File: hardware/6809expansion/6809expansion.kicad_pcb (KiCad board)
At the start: 2 copper layers, 99.7 x 99.7 mm, 13 parts, among them J0 SS50-LIKE, J1 SS50-LIKE, J2 SS50-LIKE, J3 SS50-LIKE, J4 SS50-LIKE, J5 SS50-LIKE, J6 SS50-LIKE, J7 SS50-LIKE

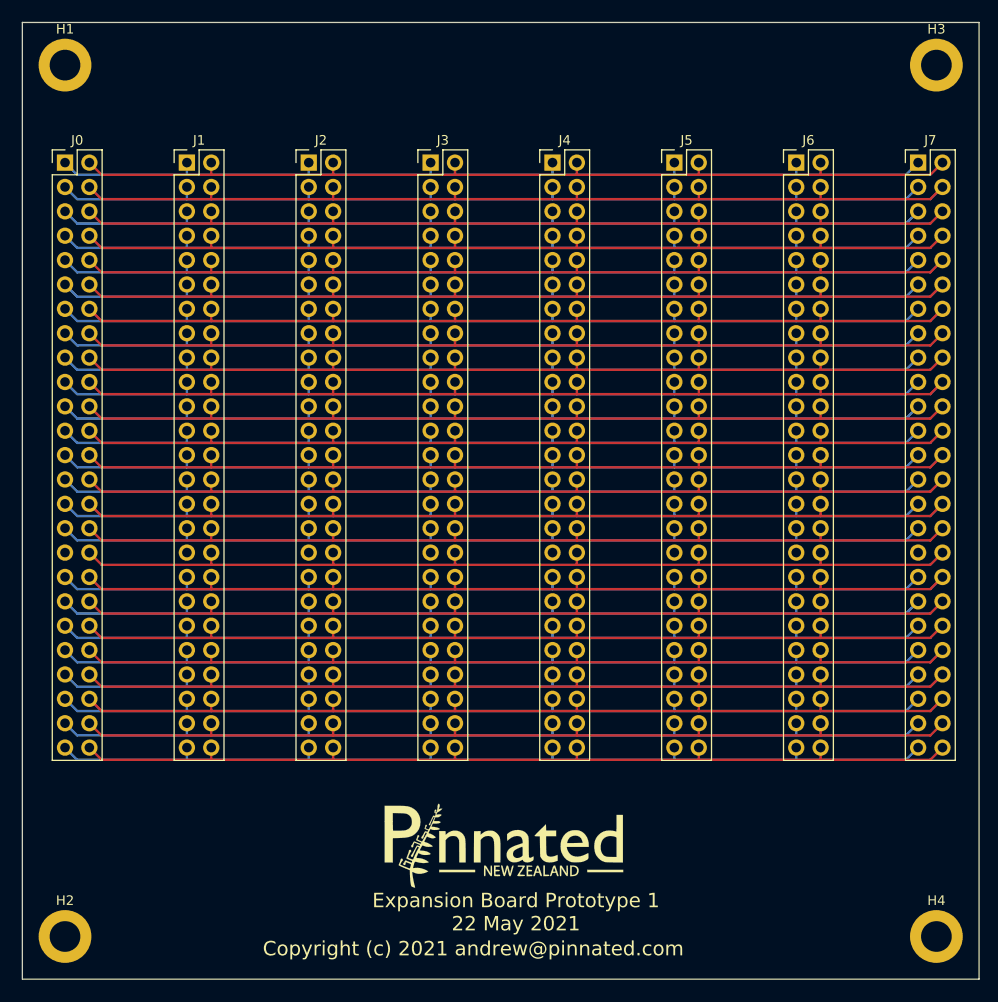
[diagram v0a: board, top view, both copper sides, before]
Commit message: finished and Gerbers generated
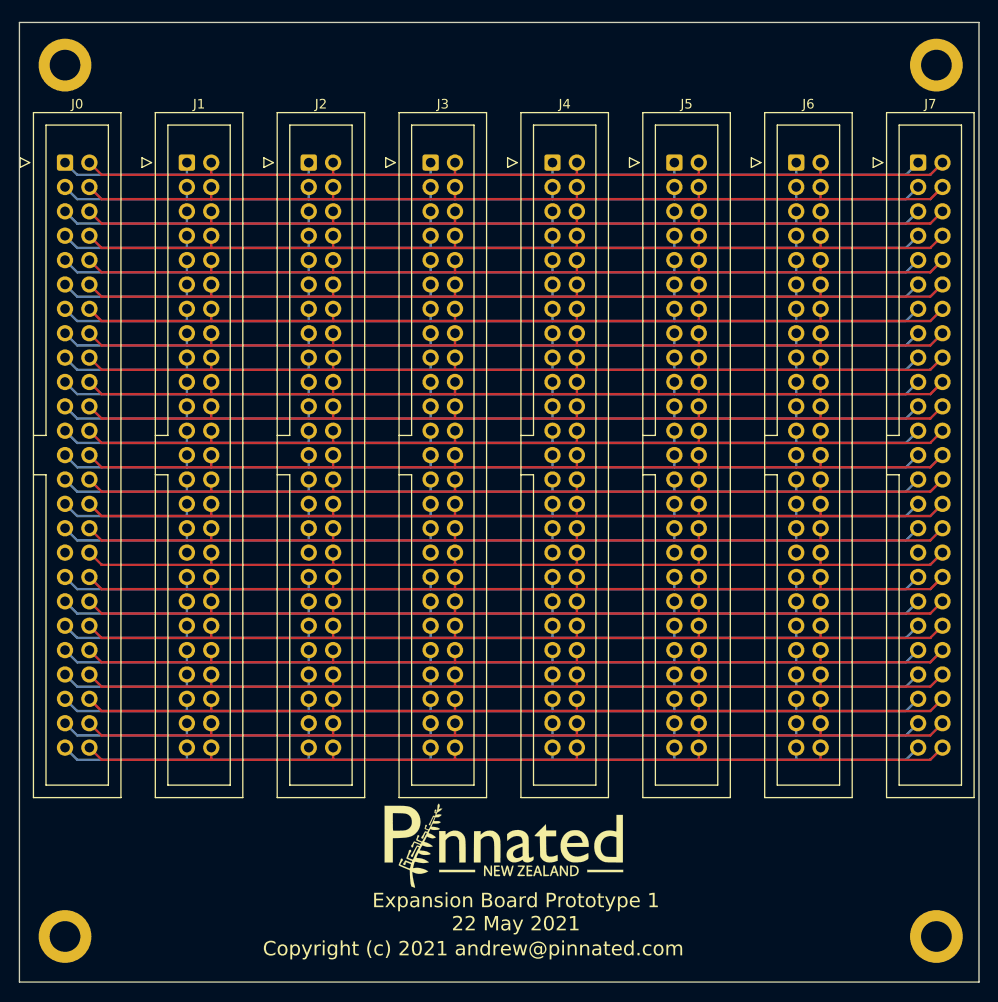
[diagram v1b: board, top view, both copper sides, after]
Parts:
- J0, J1, J2, J3, J4, J5, J6, J7: footprint Connector_PinHeader_2.54mm:PinHeader_2x25_P2.54mm_Vertical -> Connector_IDC:IDC-Header_2x25_P2.54mm_Vertical
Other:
- board size 99.7 x 99.7 mm -> 100 x 100 mm
